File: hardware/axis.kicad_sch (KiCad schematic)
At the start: 43 parts, among them J101 Cortex, J102 DX07S016JA3, SW101 SKSG, SW102 SKSG, U101 TPS78433QWDRBRQ1, U102 ATSAMD51G, U103 BMM150, U104 BHI160, Y101 32k768

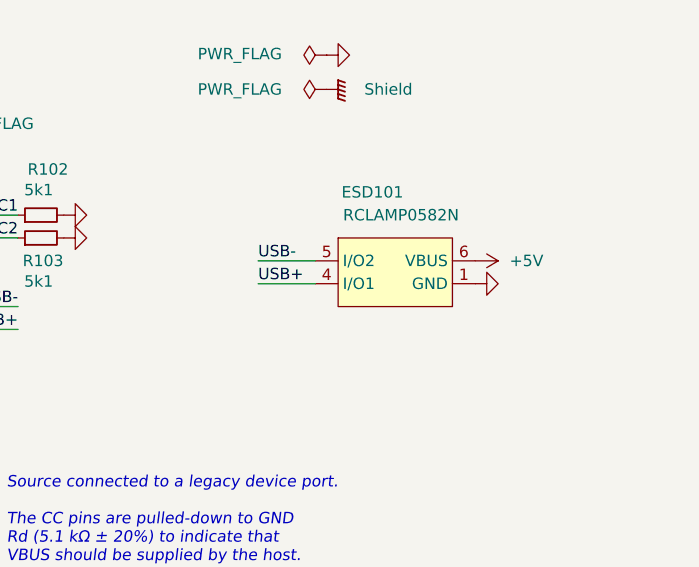
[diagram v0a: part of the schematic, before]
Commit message: Update ESD suppressor
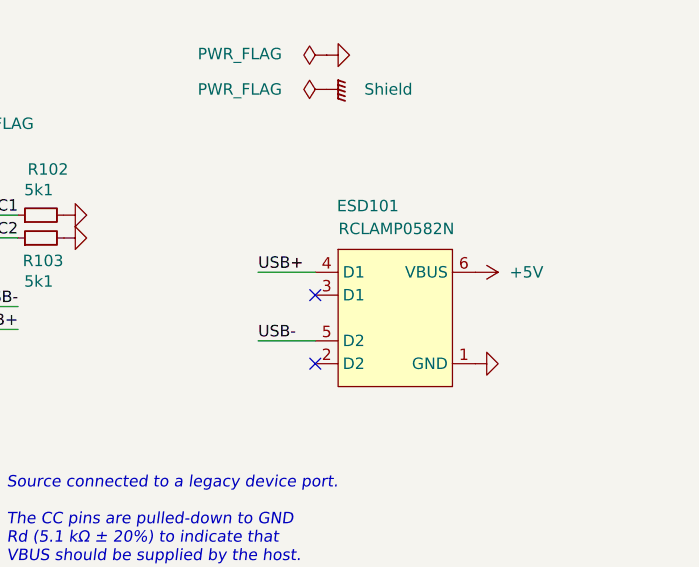
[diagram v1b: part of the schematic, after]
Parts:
- C108, C109: Manufacturer YAGEO -> TDK; Mouser 603-CC603JRNPO9BN180 -> 810-CGA3E2C0G1H180J; Product CC0603JRNPO9BN180 -> CGA3E2C0G1H180J080AA
- INFO102: value (none) -> ~
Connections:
- no-connect marks 30 -> 32
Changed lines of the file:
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@@
 	(title_block
 		(title "V2 axis")
-		(date "2026-02-25")
+		(date "2026-03-14")
 		(rev "2026-01-14")
 		(company "Versio Duo")
@@
 	)
 	(no_connect
+		(at 243.84 104.14)
+	)
+	(no_connect
 		(at 125.73 175.26)
 	)
@@
 	)
 	(no_connect
+		(at 243.84 111.76)
+	)
+	(no_connect
 		(at 59.69 96.52)
 	)
@@
 	(wire
 		(pts
+			(xy 237.49 101.6) (xy 243.84 101.6)
+		)
+		(stroke
+			(width 0)
+			(type default)
+		)
+	)
+	(wire
+		(pts
 			(xy 31.75 43.18) (xy 31.75 44.45)
 		)
@@
 	(wire
 		(pts
-			(xy 237.49 100.33) (xy 243.84 100.33)
+			(xy 237.49 109.22) (xy 243.84 109.22)
 		)
 		(stroke
@@
 	(wire
 		(pts
-			(xy 237.49 102.87) (xy 243.84 102.87)
-		)
-		(stroke
-			(width 0)
-			(type default)
-		)
-	)
-	(wire
-		(pts
 			(xy 44.45 101.6) (xy 59.69 101.6)
 		)
@@
 		)
 	)
+	(label "USB+"
+		(at 237.49 101.6 0)
+		(effects
+			(font
+				(size 1.27 1.27)
+			)
+			(justify left bottom)
+		)
+	)
 	(label "MAG-Interrupt"
 		(at 107.95 172.72 0)
@@
 		)
 	)
-	(label "USB+"
-		(at 237.49 102.87 0)
-		(effects
-			(font
-				(size 1.27 1.27)
-			)
-			(justify left bottom)
-		)
-	)
 	(label "LED-onboard"
 		(at 110.49 54.61 0)
@@
 	)
 	(label "USB-"
-		(at 237.49 100.33 0)
+		(at 237.49 109.22 0)
 		(effects
 			(font
@@
 			)
 		)
-		(property "Description" "Resistor, small symbol"
+		(property "Description" ""
 			(at 225.552 95.25 0)
 			(effects
@@
 			)
 		)
-		(property "Description" "Unpolarized capacitor, small symbol"
+		(property "Description" ""
 			(at 115.57 37.592 0)
 			(effects
@@
 	(symbol
 		(lib_id "V2_ESD_Suppressor:RCLAMP0582N")
-		(at 252.73 100.33 0)
+		(at 252.73 106.68 0)
 		(unit 1)
 		(exclude_from_sim no)
@@
 		(dnp no)
 		(property "Reference" "ESD101"
-			(at 250.19 92.71 0)
+			(at 249.682 94.234 0)
 			(effects
 				(font
@@
 		)
 		(property "Value" "RCLAMP0582N"
-			(at 253.365 95.25 0)
+			(at 252.857 96.774 0)
 			(effects
 				(font
@@
 		)
 		(property "Footprint" "V2_ESD_Suppressor:SLP1210N6"
-			(at 252.73 115.57 0)
+			(at 252.73 121.92 0)
 			(effects
 				(font
@@
 		)
 		(property "Datasheet" ""
-			(at 252.73 100.33 0)
+			(at 252.73 106.68 0)
 			(effects
 				(font
@@
 		)
 		(property "Description" ""
-			(at 252.73 100.33 0)
+			(at 252.73 106.68 0)
 			(effects
 				(font
@@
 		)
 		(property "Mouser" "947-RCLAMP0582N.TCT"
-			(at 252.73 119.38 0)
+			(at 252.73 125.73 0)
 			(effects
 				(font
@@
 		)
 		(property "Product" "RCLAMP0582N.TCT"
-			(at 252.73 123.19 0)
+			(at 252.73 129.54 0)
 			(effects
 				(font
@@
 		)
 		(property "Manufacturer" "Semtech"
-			(at 252.73 120.65 0)
+			(at 252.73 127 0)
 			(effects
 				(font
@@
 			)
 		)
-		(property "Description" "Unpolarized capacitor, small symbol"
+		(property "Description" ""
 			(at 148.59 178.562 0)
 			(effects
@@
 			)
 		)
-		(property "Description" "Push button switch, generic, two pins"
+		(property "Description" "Push button"
 			(at 254 29.21 0)
 			(effects
@@
 			)
 		)
-		(property "Description" "Resistor, small symbol"
+		(property "Description" ""
 			(at 33.02 169.672 0)
 			(effects
@@
 	(symbol
 		(lib_id "V2_power:+5V")
-		(at 261.62 100.33 270)
+		(at 261.62 101.6 270)
 		(unit 1)
 		(exclude_from_sim no)
@@
 		(on_board yes)
 		(dnp no)
-		(fields_autoplaced yes)
 		(property "Reference" "#PWR123"
-			(at 257.81 100.33 0)
+			(at 257.81 101.6 0)
 			(effects
 				(font
@@
 		)
 		(property "Value" "+5V"
-			(at 265.43 100.3299 90)
+			(at 265.43 101.5999 90)
 			(effects
 				(font
@@
 		)
 		(property "Footprint" ""
-			(at 261.62 100.33 0)
+			(at 261.62 101.6 0)
 			(effects
 				(font
@@
 		)
 		(property "Datasheet" ""
-			(at 261.62 100.33 0)
+			(at 261.62 101.6 0)
 			(effects
 				(font
@@
 		)
 		(property "Description" ""
-			(at 261.62 100.33 0)
+			(at 261.62 101.6 0)
 			(effects
 				(font
@@
 			)
 		)
-		(property "Description" "Light emitting diode, small symbol"
+		(property "Description" ""
 			(at 127 54.61 0)
 			(effects
@@
 			)
 		)
-		(property "Description" "Unpolarized capacitor, small symbol"
+		(property "Description" ""
 			(at 205.74 56.642 0)
 			(effects
@@
 			)
 		)
-		(property "Description" "Resistor, small symbol"
+		(property "Description" ""
 			(at 83.82 179.832 0)
 			(effects
@@
 			)
 		)
-		(property "Description" "Resistor, small symbol"
+		(property "Description" ""
 			(at 30.48 169.672 0)
 			(effects
@@
 			)
 		)
-		(property "Description" "Unpolarized capacitor, small symbol"
+		(property "Description" ""
 			(at 180.34 56.642 0)
 			(effects
@@
 			)
 		)
-		(property "Value" ""
+		(property "Value" "~"
 			(at 176.53 175.26 0)
 			(effects
@@
 			)
 		)
-		(property "Description" "Two pin crystal, small symbol"
+		(property "Description" ""
 			(at 34.29 43.18 0)
 			(effects
@@
 			)
 		)
-		(property "Description" "Unpolarized capacitor, small symbol"
+		(property "Description" ""
 			(at 36.83 60.452 0)
 			(effects
@@
 			)
 		)
-		(property "Mouser" "603-CC603JRNPO9BN180"
+		(property "Mouser" "810-CGA3E2C0G1H180J"
 			(at 36.83 64.516 0)
 			(effects
@@
 			)
 		)
-		(property "Product" "CC0603JRNPO9BN180"
+		(property "Product" "CGA3E2C0G1H180J080AA"
 			(at 36.83 67.564 0)
 			(effects
@@
 			)
 		)
-		(property "Manufacturer" "YAGEO"
+		(property "Manufacturer" "TDK"
 			(at 36.83 64.77 0)
 			(effects
@@
 			)
 		)
-		(property "Description" "Unpolarized capacitor, small symbol"
+		(property "Description" ""
 			(at 63.5 37.592 0)
 			(effects
@@
 			)
 		)
-		(property "Description" "Unpolarized capacitor, small symbol"
+		(property "Description" ""
 			(at 31.75 60.452 0)
 			(effects
@@
 			)
 		)
-		(property "Mouser" "603-CC603JRNPO9BN180"
+		(property "Mouser" "810-CGA3E2C0G1H180J"
 			(at 31.75 64.516 0)
 			(effects
@@
 			)
 		)
-		(property "Product" "CC0603JRNPO9BN180"
+		(property "Product" "CGA3E2C0G1H180J080AA"
 			(at 31.75 67.564 0)
 			(effects
@@
 			)
 		)
-		(property "Manufacturer" "YAGEO"
+		(property "Manufacturer" "TDK"
 			(at 31.75 64.77 0)
 			(effects
@@
 			)
 		)
-		(property "Description" "Unpolarized capacitor, small symbol"
+		(property "Description" ""
 			(at 78.232 168.91 0)
 			(effects
@@
 			)
 		)
-		(property "Description" "Resistor, small symbol"
+		(property "Description" ""
 			(at 146.812 54.61 0)
 			(effects
@@
 	(symbol
 		(lib_id "V2_power:GND")
-		(at 261.62 102.87 90)
+		(at 261.62 111.76 90)
 		(unit 1)
 		(exclude_from_sim no)
@@
 		(fields_autoplaced yes)
 		(property "Reference" "#PWR124"
-			(at 267.97 102.87 0)
+			(at 267.97 111.76 0)
 			(effects
 				(font
@@
 		)
 		(property "Value" "GND"
-			(at 265.43 102.8699 90)
+			(at 265.43 111.7599 90)
 			(effects
 				(font
@@
 		)
 		(property "Footprint" ""
-			(at 261.62 102.87 0)
+			(at 261.62 111.76 0)
 			(effects
 				(font
@@
 		)
 		(property "Datasheet" ""
-			(at 261.62 102.87 0)
+			(at 261.62 111.76 0)
 			(effects
 				(font
@@
 		)
 		(property "Description" ""
-			(at 261.62 102.87 0)
+			(at 261.62 111.76 0)
 			(effects
 				(font
@@
 			)
 		)
-		(property "Description" "Unpolarized capacitor, small symbol"
+		(property "Description" ""
 			(at 105.41 37.592 0)
 			(effects
@@
 			)
 		)
-		(property "Description" "Unpolarized capacitor, small symbol"
+		(property "Description" ""
 			(at 85.09 37.592 0)
 			(effects
@@
 			)
 		)
-		(property "Description" "Resistor, small symbol"
+		(property "Description" ""
 			(at 225.552 97.79 0)
 			(effects
@@
 			)
 		)
-		(property "Description" "Push button switch, generic, two pins"
+		(property "Description" "Push button"
 			(at 128.27 76.2 0)
 			(effects
@@
 			)
 		)
-		(property "Description" "Resistor, small symbol"
+		(property "Description" ""
 			(at 86.36 179.832 0)
 			(effects
@@
 			)
 		)
-		(property "Description" "Unpolarized capacitor, small symbol"
+		(property "Description" ""
 			(at 64.77 164.592 0)
 			(effects
@@
 			)
 		)
-		(property "Description" "Unpolarized capacitor, small symbol"
+		(property "Description" ""
 			(at 95.25 37.592 0)
 			(effects
@@
 			)
 		)
-		(property "Description" "Resistor, small symbol"
+		(property "Description" ""
 			(at 69.342 123.19 0)
 			(effects

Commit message: KiCad 10
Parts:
- INFO102: value ~ -> (none)

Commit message: Update
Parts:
- C101, C102, C103, C104, C105, C106, C107, C110, C111: Id (none) -> Capacitor:${SYMBOL_NAME}
- C108, C109: Id (none) -> Capacitor:${SYMBOL_NAME}; Rating (none) -> 50V
- C112: Id (none) -> Capacitor:${SYMBOL_NAME}; Manufacturer YAGEO -> TDK; Mouser 603-CC0603JR6BB474 -> 810-CGA3E3X7R1H474KB; Product CC0603JRX7R6BB474 -> CGA3E3X7R1H474K080AB; Rating (none) -> 50V
- D101, D102: Id (none) -> LED:${SYMBOL_NAME}
- D103: Id (none) -> LED:${SYMBOL_NAME}; Rating (none) -> 605nm
- ESD101: Id (none) -> ESD:${SYMBOL_NAME}
- J102: Id (none) -> USB:${SYMBOL_NAME}; Rating (none) -> USB2.0
- R101, R102, R103, R104, R105, R106, R107, R108: Id (none) -> Resistor:${SYMBOL_NAME}
- SW101, SW102: Id (none) -> Button:${SYMBOL_NAME}; Rating (none) -> 1.6N
- U101: Id (none) -> LDO:${SYMBOL_NAME}
- U102: Id (none) -> MCU:${SYMBOL_NAME}
- U103: Id (none) -> Compass:${SYMBOL_NAME}
- U104: Id (none) -> IMU:${SYMBOL_NAME}
- Y101: Id (none) -> Crystal:${SYMBOL_NAME}
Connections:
- net VDDCORE renamed +VDDCORE

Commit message: Update
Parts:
- D101, D102: Rating (none) -> 15mA
- D103: Rating 605nm -> 605nm
- U101: Rating (none) -> 300mA
- Y101: Rating (none) -> 10ppm
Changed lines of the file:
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@@
 	(title_block
 		(title "V2 axis")
-		(date "2026-03-20")
+		(date "2026-04-10")
 		(rev "2026-01-14")
 		(company "Versio Duo")
@@
 			)
 		)
-		(property "Rating" " 605nm "
+		(property "Rating" "605nm"
 			(at 127 36.83 0)
 			(hide yes)
@@
 			)
 		)
+		(property "Rating" "15mA"
+			(at 250.19 77.47 0)
+			(hide yes)
+			(show_name no)
+			(do_not_autoplace no)
+			(effects
+				(font
+					(size 1.27 1.27)
+				)
+			)
+		)
 		(pin "1"
 		)
@@
 			)
 		)
+		(property "Rating" "300mA"
+			(at 193.04 92.71 0)
+			(hide yes)
+			(show_name no)
+			(do_not_autoplace no)
+			(effects
+				(font
+					(size 1.27 1.27)
+				)
+			)
+		)
 		(pin "1"
 		)
@@
 			)
 		)
+		(property "Rating" "15mA"
+			(at 267.97 77.47 0)
+			(hide yes)
+			(show_name no)
+			(do_not_autoplace no)
+			(effects
+				(font
+					(size 1.27 1.27)
+				)
+			)
+		)
 		(pin "1"
 		)
@@
 			)
 		)
+		(property "Rating" "10ppm"
+			(at 34.29 67.31 0)
+			(hide yes)
+			(show_name no)
+			(do_not_autoplace no)
+			(effects
+				(font
+					(size 1.27 1.27)
+				)
+			)
+		)
 		(pin "1"
 		)
@@
 			(name "V2_A4.kicad_wks")
 			(type worksheet)
-			(data |KLUv/WBhBk0QALbYTiEQtRsmZc5q276ayLS71D6kxbkmoTeIJM7lAHtEAMAAxQFGAD8ARQCbvIHa
-				a/wrVHSazXnPhvzar1BNtH1kxRf5EwCAQPh5F+e0kJq0nmtfKDvj37Jf3xQUlFKqztoXWzE7iAAI
-				iJ6Q5m2d9RAC9jcPPWe/GXf/9ewpPR3+uPbv7bdzvr37wXlr2X8dBHFXu7Z3HUG7Kvrz9qKU7eB2
-				v/MM4n/Mhfg5G5sn7WsDTS2mA1WyssZDsy4YdpEGzfD8Ny+85JzH7H+961FjX/x0qtq0MdaqJ8dx
-				k1KAwF+soV3VFnEoqewX+XNfTaqqPatRlLsbgcKhzs5+29sEzSaWRPZ4txDEjpmZNCoSiiMhaUwy
-				y4Jg3oe5pmhPRSS7MtJAerbfnYNNgaEkuCg6oVzYhbEsF1vRgtxS55zTIVig4URjFFJTI1qYFNIB
-				YESmRusYYvaiF0uSUdhu1Q2lFiOgdmN7VvaH2oWyw9MQXRuZtQQQoIsxFn2ldtnpQiUNa0HvDQCK
-				f/XTisCgEJQEXe/if4EJsakkqj8BMmGAU+ZM/AG8LSEJMfgkOKfSKPhw4rD3ZHfmNZYNfDMigEPJ
-				EBoIDghtm1kJ8BAQ8xyGdkOuFQy33sishFt8DZNX4uNRXJZ5hBy746RJaNtgbfyB613d0dov6Cdg
-				iUQT9BXkf9EiYDuODpB6gKkC|
+			(data |KLUv/WD5BbUPADbXSyEA1TbWikhSlOA2eC2ekVMEUCwq7NEwtcLUrO9RVbWigglBAD0ARQB3rDJr
+				Vfe8iEc347HKLOu3hM0n3acAgEAZ+mtWq1rqUSxebyypb/3fvvl2Ks1ai1318qyxua+IAgRM0MgT
+				vxCDqNazy01dUkv9SffBzyqWXV6zk7TDjC//75ZXzHffvHX4Y/Xf35uU+iW//OHdpP7XYKnf08G7
+				Ws+4sz/Se05W5tbSsFNFN3RTUXTjhdPWNR7ehuG4iIngvhBQHGxi+IlSiXCRzHYxEfbe576fb+gn
+				B78Z+mSX28Z5ZV5BEKwWAwQ+a06BCmH90rZJg9JtG4SrtqNsE+pn/kpSOzSUhmVScSgcO1gJcdSg
+				J6zLuq1W1TZJF+moiP3v9XDUP1+S1KFCs7SB4TTQalSg4UCjGDM0M3GaNAZgZObmWAewpQGB0gB3
+				GYWe0WuYLYxil2+HCVPCLoewmMo8a9CJow+hHPOLKHdUb0wU8lRpRE+qFdAXJgbU7nMwecZYivJQ
+				iTgLkNig5tH7xtAJA8QyZ+ZP4GUJKSTwm+RM51H7yWknvCe7YZZxrISdEQ48yLJBiQaevBZD1kY4
+				h0V7Dqlt/1rBcP0NQy83g9hYapcpANydipsbWw09qO7ggsG8qpSEBRoltBf/e9cTMh29AaQeYKo=|
 			)
-			(checksum "0A61268C685EAF945CA2EA8187370BD3")
+			(checksum "080A27BD1FADC1F81518BF82EA92C143")
 		)
 	)

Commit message: Update
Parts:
- ESD101: Rating (none) -> 20kV
- U102: Rating (none) -> Cortex-M4F
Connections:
- net +VDDCORE renamed +VCORE
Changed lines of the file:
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@@
 	(title_block
 		(title "V2 axis")
-		(date "2026-04-10")
+		(date "2026-04-14")
 		(rev "2026-01-14")
 		(company "Versio Duo")
@@
 		)
 	)
-	(label "+VDDCORE"
+	(label "+VCORE"
 		(at 63.5 21.59 0)
 		(effects
@@
 			)
 		)
+		(property "Rating" "20kV"
+			(at 252.73 135.89 0)
+			(hide yes)
+			(show_name no)
+			(do_not_autoplace no)
+			(effects
+				(font
+					(size 1.27 1.27)
+				)
+			)
+		)
 		(pin "1"
 		)
@@
 		(unit 1)
 		(body_style 1)
-		(exclude_from_sim yes)
+		(exclude_from_sim no)
 		(in_bom no)
 		(on_board yes)
@@
 			)
 		)
+		(property "Sim.Enable" "0"
+			(at 234.95 152.4 0)
+			(hide yes)
+			(show_name no)
+			(do_not_autoplace no)
+			(effects
+				(font
+					(size 1.27 1.27)
+				)
+			)
+		)
 		(instances
 			(project "axis"
@@
 			)
 		)
+		(property "Rating" "Cortex-M4F"
+			(at 76.2 158.75 0)
+			(hide yes)
+			(show_name no)
+			(do_not_autoplace no)
+			(effects
+				(font
+					(size 1.27 1.27)
+				)
+			)
+		)
 		(pin "1"
 			(alternate "XIN32")
@@
 		(unit 1)
 		(body_style 1)
-		(exclude_from_sim yes)
+		(exclude_from_sim no)
 		(in_bom no)
 		(on_board yes)
@@
 			(at 176.53 165.1 0)
 			(hide yes)
+			(show_name no)
+			(do_not_autoplace no)
+			(effects
+				(font
+					(size 1.27 1.27)
+				)
+			)
+		)
+		(property "Sim.Enable" "0"
+			(at 176.53 165.1 0)
+			(hide yes)

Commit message: Update DRC
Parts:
- renumbered C108 to C101, C109 to C102, C101 to C103, C110 to C104, C112 to C105, C102 to C106, C103 to C107, C104 to C108, C105 to C109, C111 to C110, C106 to C111, C107 to C112, D103 to D101, D101 to D102, D102 to D103, INFO102 to INFO101, INFO101 to INFO102, R105 to R101, R106 to R102, R104 to R103, R107 to R104, R108 to R105, R101 to R106, R102 to R107, R103 to R108, SW102 to SW101, SW101 to SW102, U104 to U101, U101 to U104
